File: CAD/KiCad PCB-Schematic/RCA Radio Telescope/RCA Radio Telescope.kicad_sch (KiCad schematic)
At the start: 2 parts, among them U1 ZX60-P33ULN+

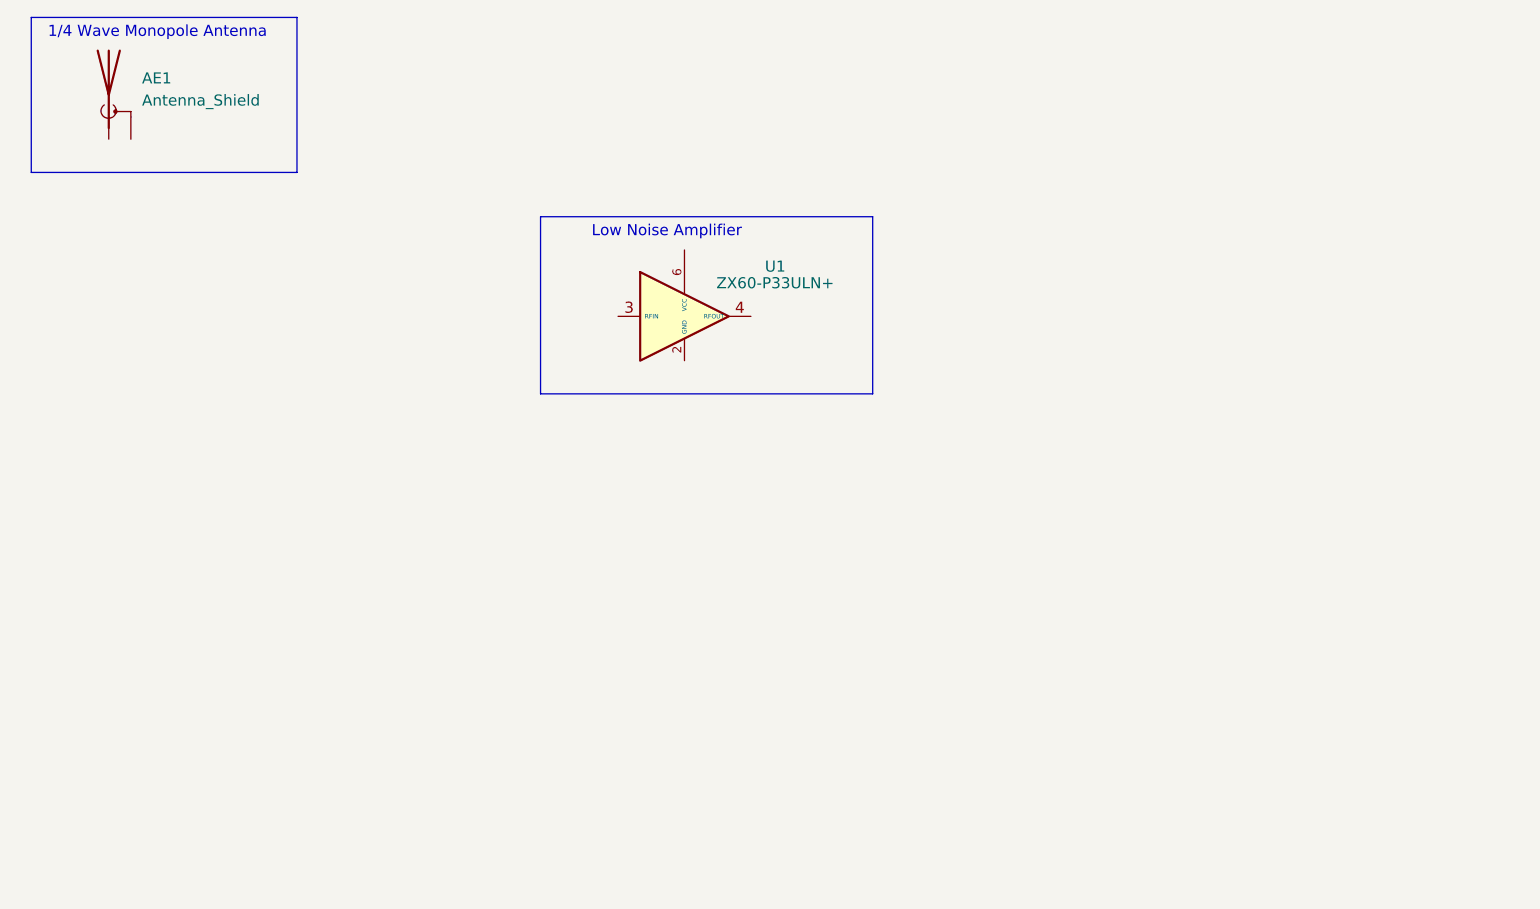
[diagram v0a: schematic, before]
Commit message: Updated Schematic
Added SDR, Battery (incomplete)
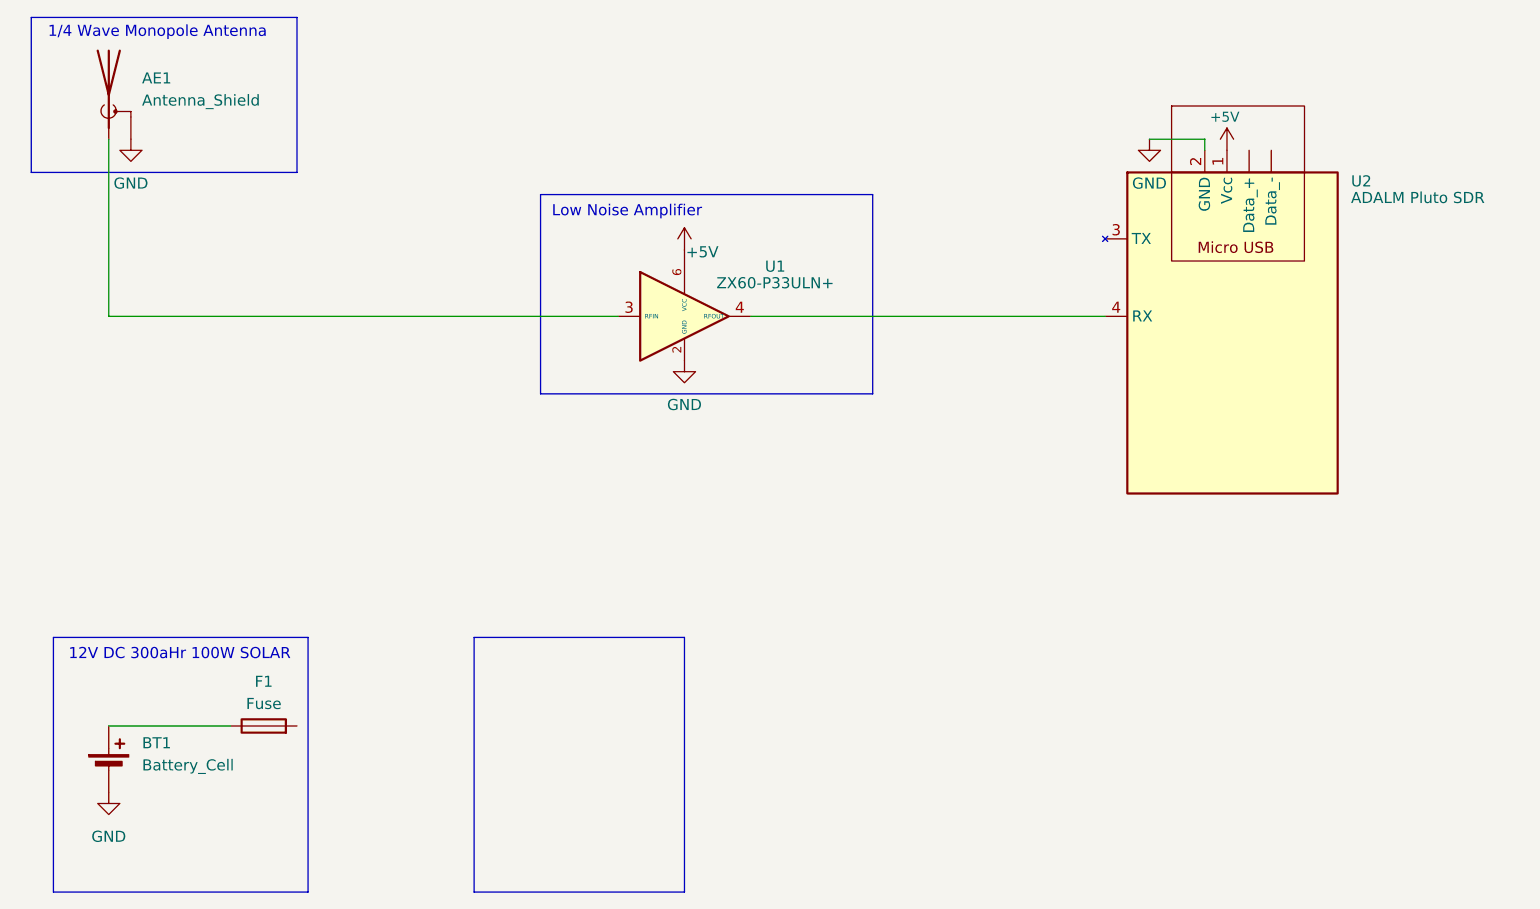
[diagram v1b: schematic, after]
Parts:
- added BT1: Battery_Cell, symbol Device:Battery_Cell
- added F1: Fuse, symbol Device:Fuse
- added U2: ADALM Pluto SDR, symbol Radio Telescope:ADALM_Pluto_SDR
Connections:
- net GND: now reaches U1.2 (GND), U1.5 (GND)
- net GND: now also AE1.2 (Shield), BT1.2 (-), U2.2 (GND)
- net at U1.3 (RFIN): now also AE1.1 (A)
- net at U1.4 (RFOUT): now also U2.4 (RX)
- net +5V: now reaches U1.6 (VCC)
- net +5V: now also U2.1 (Vcc)
- new net: BT1.1 (+), F1.1
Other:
- note added: "12V DC 300aHr 100W SOLAR"

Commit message: Updated Schematic
Updated schematic with buck board, and  foundation for Power Over Ethernet.
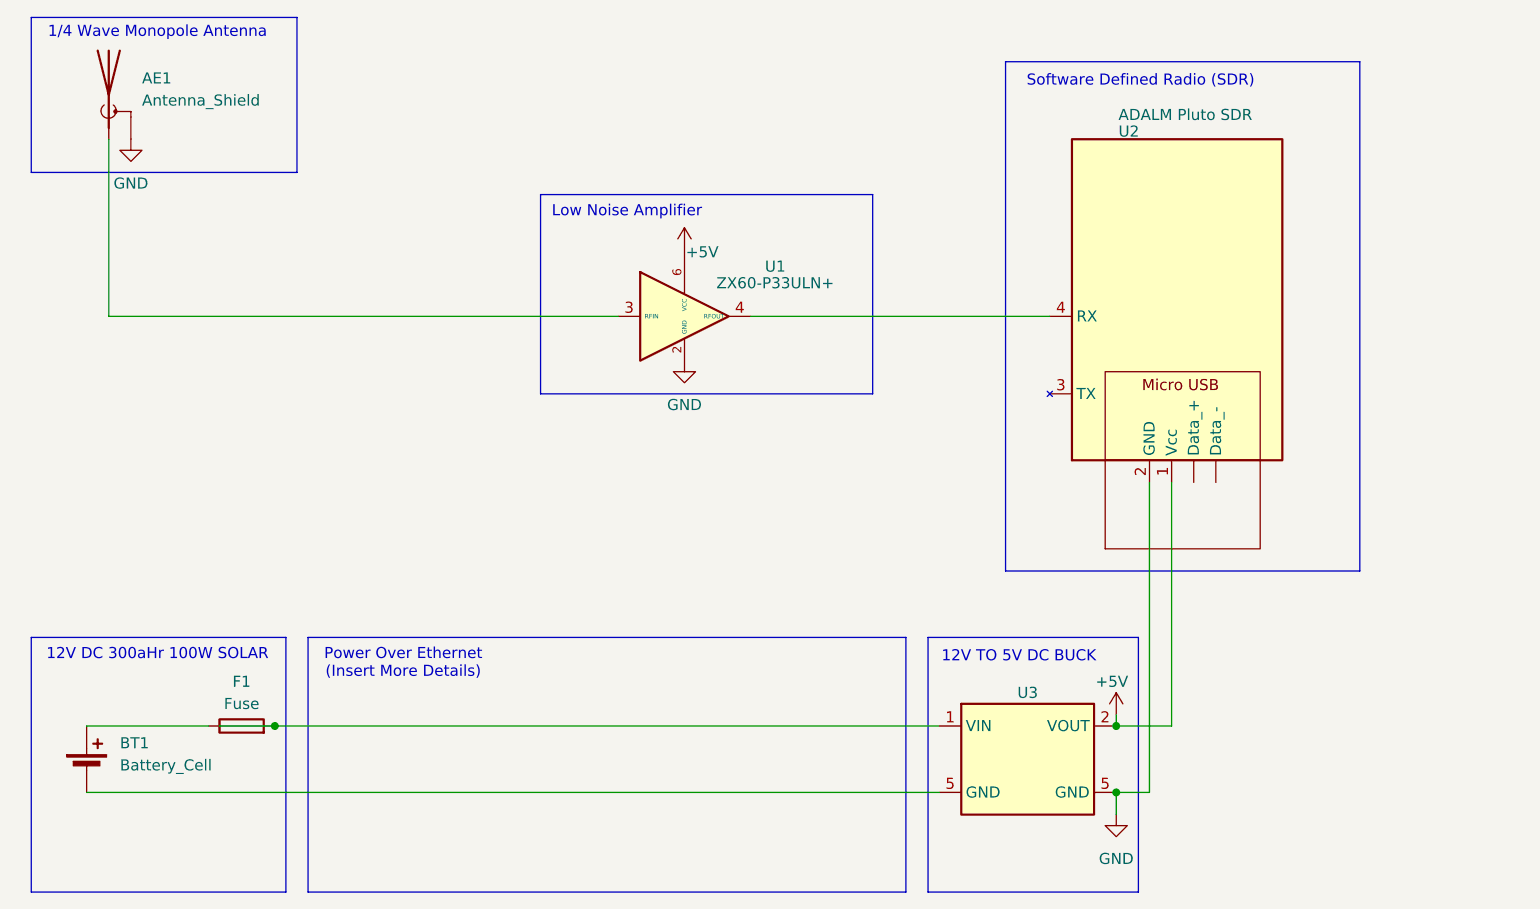
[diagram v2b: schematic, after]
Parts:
- added U3: ~, symbol Radio Telescope:12vTo5vDC
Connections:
- net +5V: now also U3.2 (VOUT)
- net GND: now also U3.5 (GND); no longer BT1.2 (-)
- net at F1.2: now also U3.1 (VIN)
- new net: BT1.2 (-), U3.5 (GND)
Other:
- note added: "12V TO 5V DC BUCK"
- note added: "Power Over Ethernet (Insert More Details)"
- note added: "Software Defined Radio (SDR)"
- moved on the sheet: BT1, F1, U2

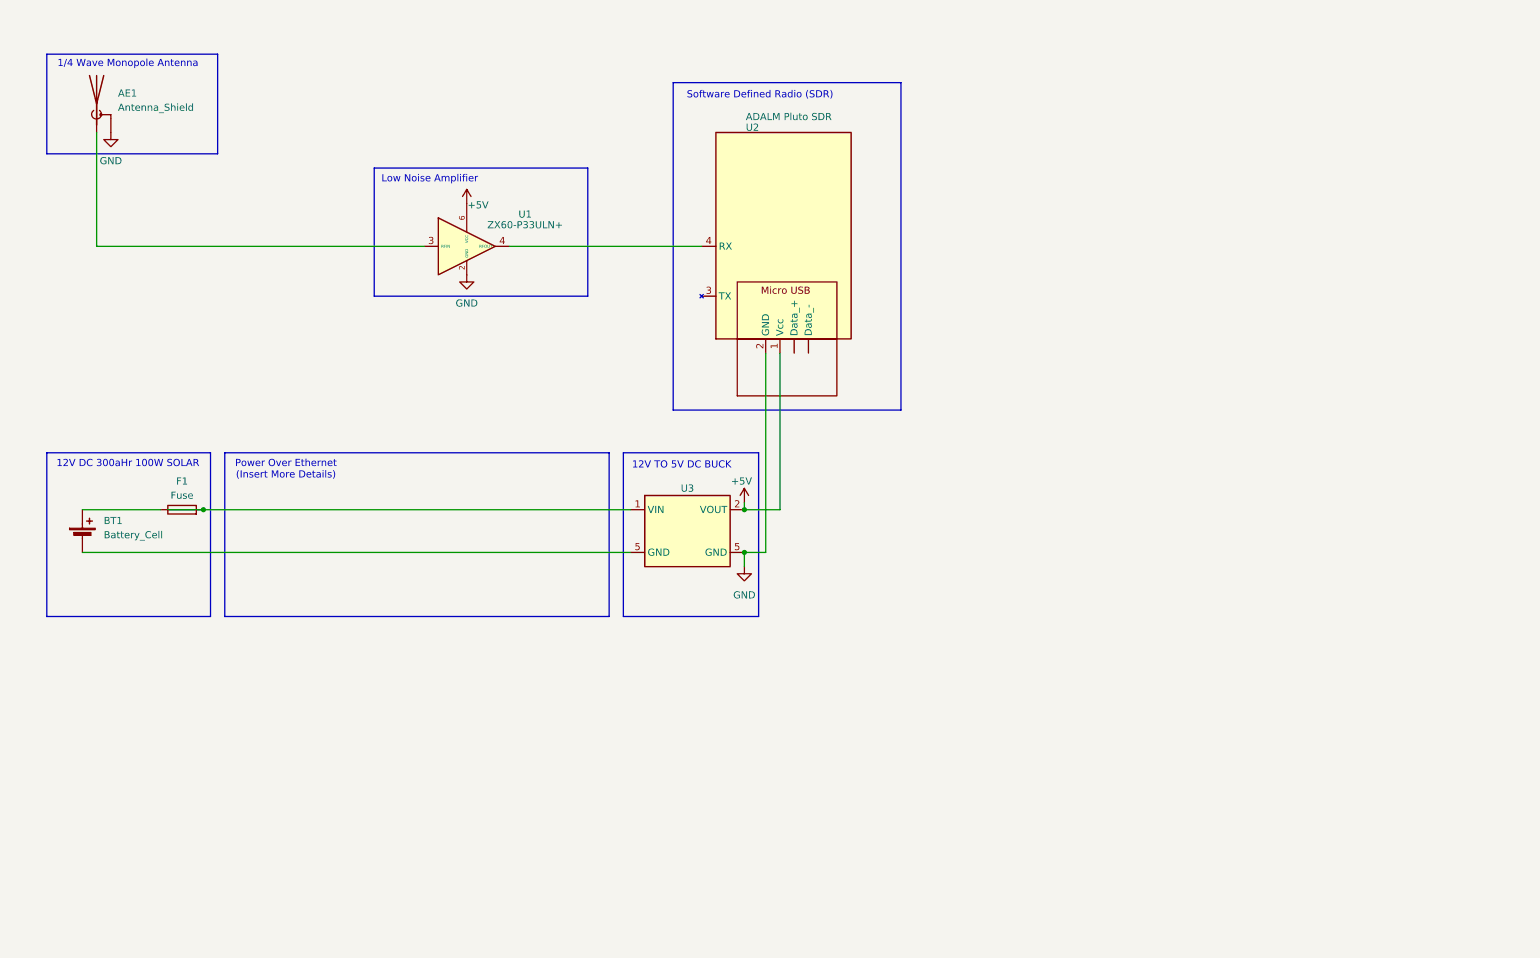
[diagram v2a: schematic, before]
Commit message: Updated Schematic to v1.1
- Added PoE, Power Supply components
- Laid out components on base side
- Added details about voltages for PoE
- Updated and added symbols for Pluto, Ethernet Dongle, PoE Injector/Splitter, and Boost Converter
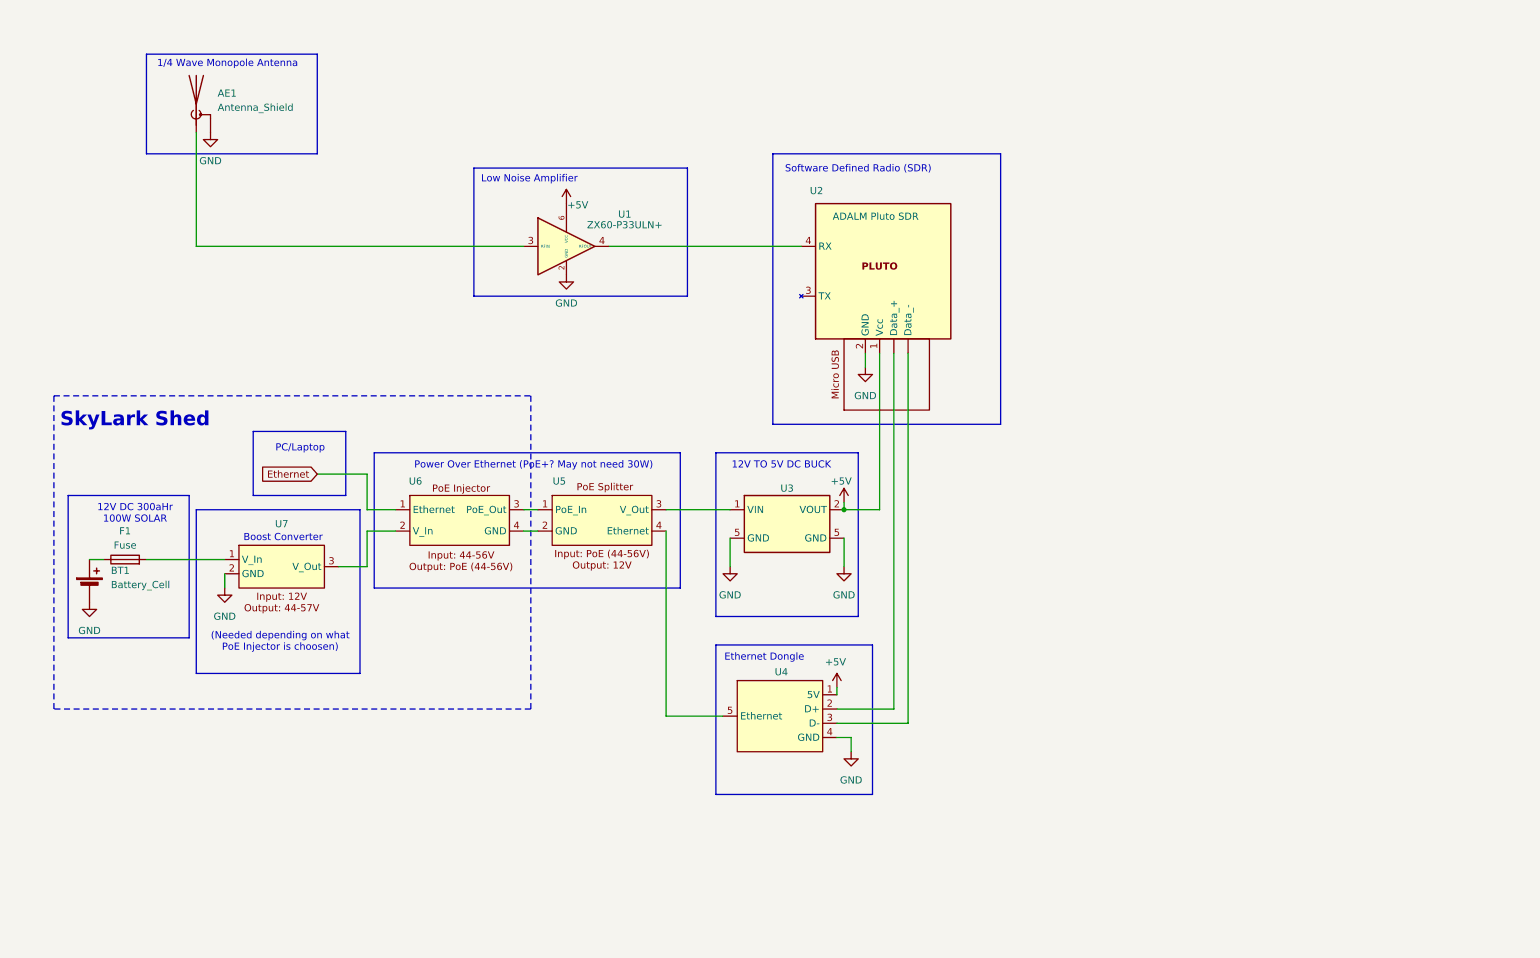
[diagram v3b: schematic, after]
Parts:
- added U4: ~, symbol Radio Telescope:Ethernet_Dongle
- added U5: ~, symbol Radio Telescope:PoE_Spliter
- added U6: ~, symbol Radio Telescope:PoE_Injector
- added U7: ~, symbol Radio Telescope:Boost_Converter
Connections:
- net +5V: now also U4.1 (5V)
- net GND: now also BT1.2 (-), U4.4 (GND), U7.2 (GND)
- net at U2. (Data_-): now also U4.3 (D-)
- net at U3.1 (VIN): now also U5.3 (V_Out); no longer F1.2
- new net: U2. (Data_-), U4.2 (D+)
- new net: U5.1 (PoE_In), U6.3 (PoE_Out)
- new net: U5.2 (GND), U6.4 (GND)
- new net: U4.5 (Ethernet), U5.4 (Ethernet)
- new net: F1.2, U7.1 (V_In)
- new net: U6.2 (V_In), U7.3 (V_Out)
- new net Ethernet: U6.1 (Ethernet)
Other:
- note added: "(Needed depending on what PoE Injector is choosen)"
- note added: "Boost Converter"
- note added: "Ethernet Dongle"
- note added: "PC/Laptop"
- note added: "Power Over Ethernet (PoE+? May not need 30W)"
- note added: "SkyLark Shed"
- note removed: "Power Over Ethernet (Insert More Details)"
- moved on the sheet: AE1, BT1, F1, U1, U2, U3

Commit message: Update Schematic to Version 1.2
- Removed Buck Converter
- Added Section for Step Down (need to find one that is good and can provide smooth voltage)
- Added USB schematic symbols
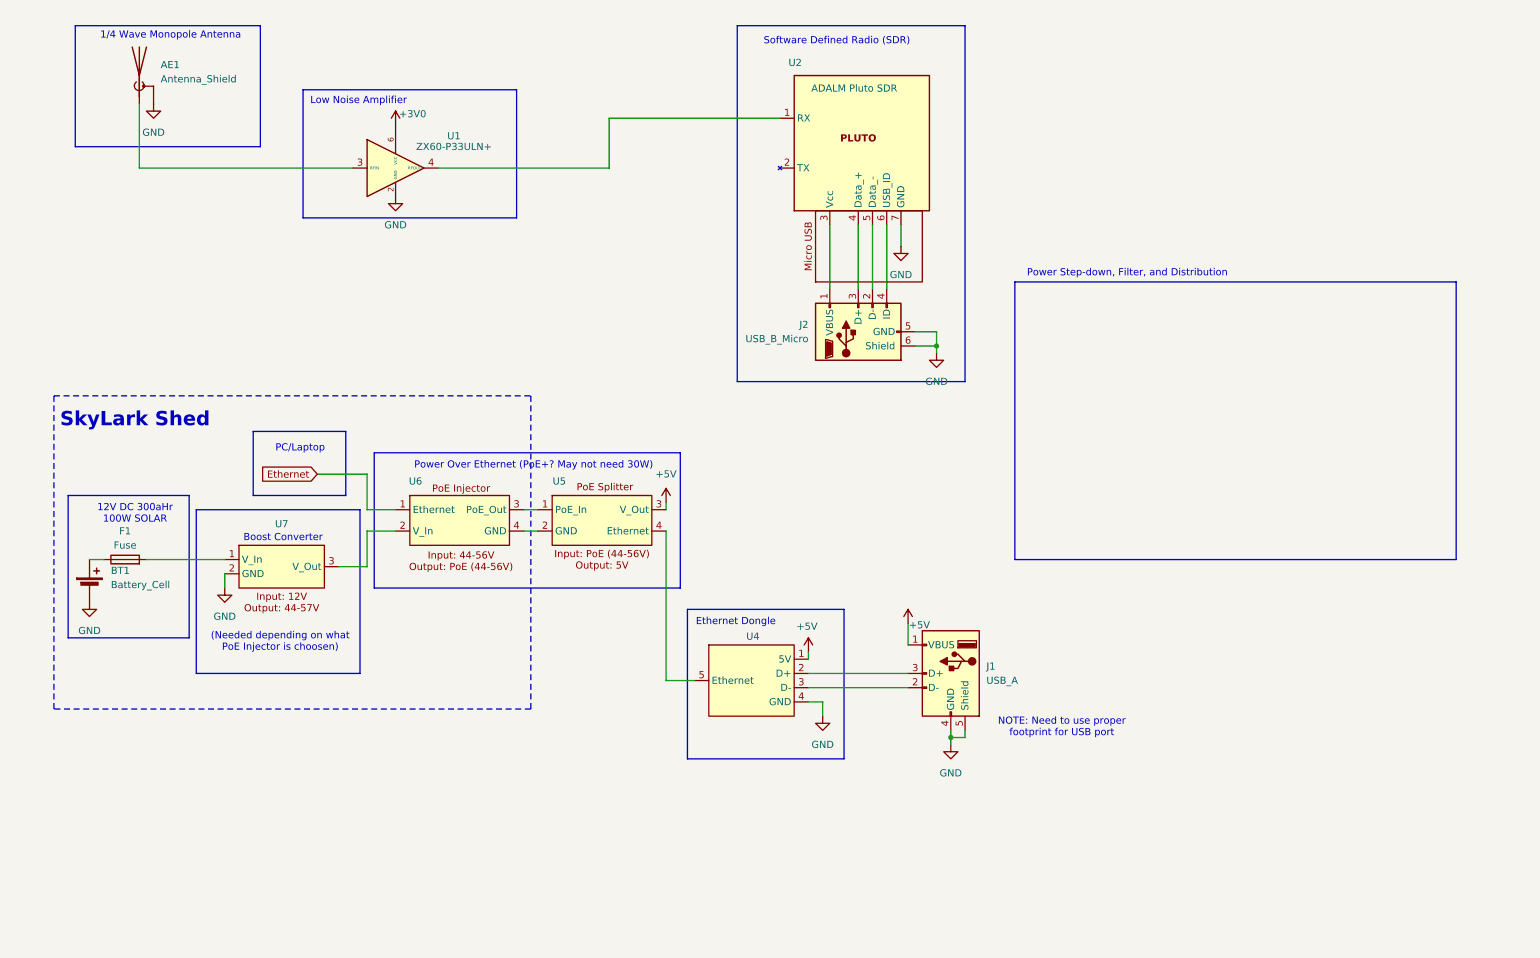
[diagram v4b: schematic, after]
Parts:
- removed U3: ~, symbol Radio Telescope:12vTo5vDC
- added J1: USB_A, symbol Connector:USB_A
- added J2: USB_B_Micro, symbol Connector:USB_B_Micro
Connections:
- net +5V: now also U5.3 (V_Out), J1.1 (VBUS); no longer U1.6 (VCC), U2.1 (Vcc)
- net GND: now also U2.7 (GND), J1.4 (GND), J1.5 (Shield), J2.5 (GND), J2.6 (Shield); no longer U2.2 (GND)
- net at U4.2 (D+): now also J1.3 (D+); no longer U2. (Data_-)
- net at U4.3 (D-): now also J1.2 (D-); no longer U2. (Data_-)
- net at U2.3 (Vcc): now also J2.1 (VBUS)
- net at U1.4 (RFOUT): now also U2.1 (RX); no longer U2.4 (RX)
- new net: J2.3 (D+), U2.4 (Data_+)
- new net: J2.2 (D-), U2.5 (Data_-)
- new net: J2.4 (ID), U2.6 (USB_ID)
- new net +3V0: U1.6 (VCC)
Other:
- note added: "NOTE: Need to use proper footprint for USB port"
- note added: "Power Step-down, Filter, and Distribution"
- note removed: "12V TO 5V DC BUCK"
- moved on the sheet: AE1, U1, U4
